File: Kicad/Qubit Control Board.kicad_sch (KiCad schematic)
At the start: 148 parts, among them J1 USB_C_Receptacle_PowerOnly_6P, J2 CLK_Pins, J3 Idata, J4 Qdata, J5 SPIdata, J6 SMA, U1 LT3045xMSE, U2 TRF372017IRGZR, U3 LT3045xMSE, U4 LT3045xMSE, U5 SN65LVDS1DBV, U6 AD9743BCPZ, Y2 CVHD-950-100.000

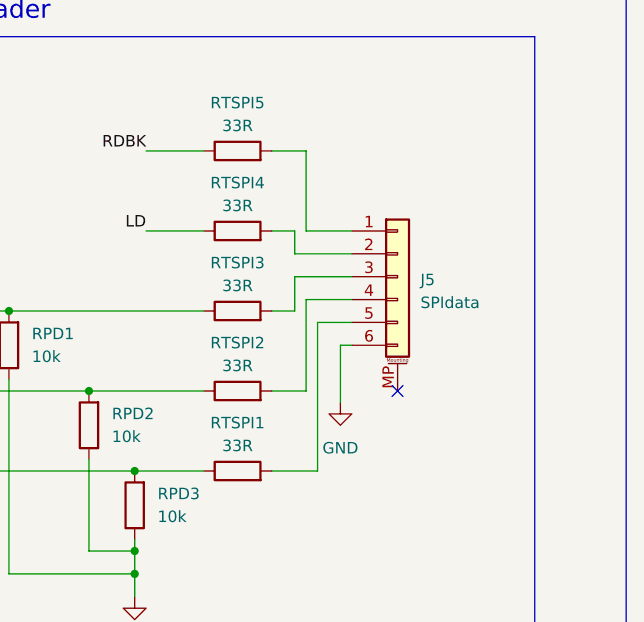
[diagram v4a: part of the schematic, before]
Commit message: Did 3.3V-B LDO routing
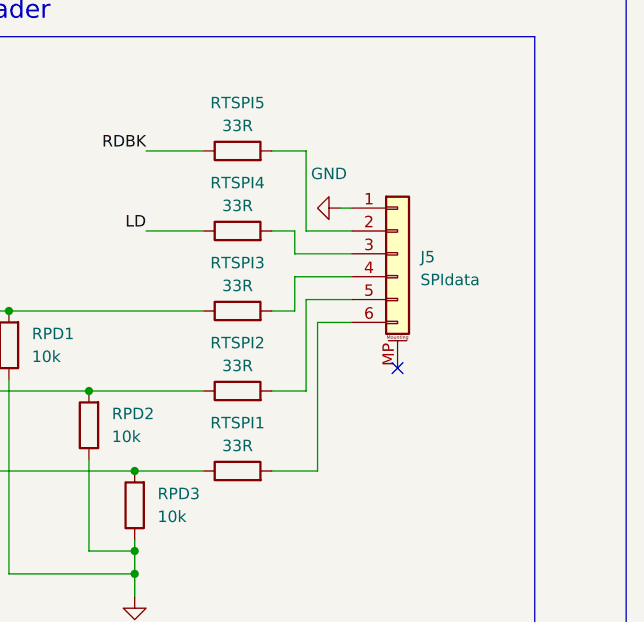
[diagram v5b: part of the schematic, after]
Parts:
- CD11, CD20, CD21, CD22, CD26: footprint Capacitor_SMD:C_0805_2012Metric_Pad1.18x1.45mm_HandSolder -> Capacitor_SMD:C_0603_1608Metric
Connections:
- net GND: now also J5.1 (Pin_1); no longer J5.6 (Pin_6)
- net at RTSPI4.2: now also J5.3 (Pin_3); no longer J5.2 (Pin_2)
- net at RTSPI5.2: now also J5.2 (Pin_2); no longer J5.1 (Pin_1)
- net at RTSPI1.2: now also J5.6 (Pin_6); no longer J5.5 (Pin_5)
- net at RTSPI3.2: now also J5.4 (Pin_4); no longer J5.3 (Pin_3)
- net at RTSPI2.2: now also J5.5 (Pin_5); no longer J5.4 (Pin_4)
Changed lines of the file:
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@@
 	)
 	(no_connect
-		(at 551.18 255.27)
+		(at 551.18 252.73)
 	)
 	(no_connect
@@
 	(wire
 		(pts
-			(xy 546.1 250.19) (xy 544.83 250.19)
-		)
-		(stroke
-			(width 0)
-			(type default)
-		)
-	)
-	(wire
-		(pts
 			(xy 238.76 210.82) (xy 246.38 210.82)
 		)
@@
 	(wire
 		(pts
+			(xy 544.83 234.95) (xy 546.1 234.95)
+		)
+		(stroke
+			(width 0)
+			(type default)
+		)
+	)
+	(wire
+		(pts
 			(xy 508 107.95) (xy 501.65 107.95)
 		)
@@
 	(wire
 		(pts
-			(xy 544.83 250.19) (xy 544.83 256.54)
-		)
-		(stroke
-			(width 0)
-			(type default)
-		)
-	)
-	(wire
-		(pts
 			(xy 210.82 130.81) (xy 209.55 130.81)
 		)
@@
 			)
 		)
-		(property "Footprint" "Capacitor_SMD:C_0805_2012Metric_Pad1.18x1.45mm_HandSolder"
+		(property "Footprint" "Capacitor_SMD:C_0603_1608Metric"
 			(at 374.9548 256.54 0)
 			(hide yes)
@@
 			)
 		)
-		(property "Footprint" "Capacitor_SMD:C_0805_2012Metric_Pad1.18x1.45mm_HandSolder"
+		(property "Footprint" "Capacitor_SMD:C_0603_1608Metric"
 			(at 430.8348 287.02 0)
 			(hide yes)
@@
 	)
 	(symbol
-		(lib_id "Connector_Generic_MountingPin:Conn_01x06_MountingPin")
-		(at 551.18 242.57 0)
-		(unit 1)
-		(body_style 1)
-		(exclude_from_sim no)
-		(in_bom yes)
-		(on_board yes)
-		(in_pos_files yes)
-		(dnp no)
-		(fields_autoplaced yes)
-		(property "Reference" "J5"
-			(at 553.72 242.9255 0)
-			(show_name no)
-			(do_not_autoplace no)
-			(effects
-				(font
-					(size 1.27 1.27)
-				)
-				(justify left)
-			)
-		)
-		(property "Value" "SPIdata"
-			(at 553.72 245.4655 0)
-			(show_name no)
-			(do_not_autoplace no)
-			(effects
-				(font
-					(size 1.27 1.27)
-				)
-				(justify left)
-			)
-		)
-		(property "Footprint" "Connector_PinHeader_1.00mm:PinHeader_1x06_P1.00mm_Vertical"
-			(at 551.18 242.57 0)
-			(hide yes)
-			(show_name no)
-			(do_not_autoplace no)
-			(effects
-				(font
-					(size 1.27 1.27)
-				)
-			)
-		)
-		(property "Datasheet" ""
-			(at 551.18 242.57 0)
-			(hide yes)
-			(show_name no)
-			(do_not_autoplace no)
-			(effects
-				(font
-					(size 1.27 1.27)
-				)
-			)
-		)
-		(property "Description" "Generic connectable mounting pin connector, single row, 01x06, script generated (kicad-library-utils/schlib/autogen/connector/)"
-			(at 551.18 242.57 0)
-			(hide yes)
-			(show_name no)
-			(do_not_autoplace no)
-			(effects
-				(font
-					(size 1.27 1.27)
-				)
-			)
-		)
-		(pin "5"
-		)
-		(pin "6"
-		)
-		(pin "4"
-		)
-		(pin "2"
-		)
-		(pin "3"
-		)
-		(pin "1"
-		)
-		(pin "MP"
-		)
-		(instances
-			(project "Qubit Control Board"
-				(path "/d02a9e30-46b8-444a-9e12-1a93fb154b6d"
-					(reference "J5")
-					(unit 1)
-				)
-			)
-		)
-	)
-	(symbol
 		(lib_id "power:GND")
 		(at 54.61 106.68 0)
@@
 			)
 		)
-		(property "Footprint" "Capacitor_SMD:C_0805_2012Metric_Pad1.18x1.45mm_HandSolder"
+		(property "Footprint" "Capacitor_SMD:C_0603_1608Metric"
 			(at 374.9548 287.02 0)
 			(hide yes)
@@
 			)
 		)
-		(property "Footprint" "Capacitor_SMD:C_0805_2012Metric_Pad1.18x1.45mm_HandSolder"
+		(property "Footprint" "Capacitor_SMD:C_0603_1608Metric"
 			(at 484.1748 322.58 0)
 			(hide yes)
@@
 	(symbol
 		(lib_id "power:GND")
-		(at 544.83 256.54 0)
+		(at 544.83 234.95 270)
 		(unit 1)
 		(body_style 1)
@@
 		(fields_autoplaced yes)
 		(property "Reference" "#PWR058"
-			(at 544.83 262.89 0)
+			(at 538.48 234.95 0)
 			(hide yes)
 			(show_name no)
@@
 		)
 		(property "Value" "GND"
-			(at 544.83 261.62 0)
+			(at 543.56 231.14 90)
 			(show_name no)
 			(do_not_autoplace no)
@@
 		)
 		(property "Footprint" ""
-			(at 544.83 256.54 0)
+			(at 544.83 234.95 0)
 			(hide yes)
 			(show_name no)
@@
 		)
 		(property "Datasheet" ""
-			(at 544.83 256.54 0)
+			(at 544.83 234.95 0)
 			(hide yes)
 			(show_name no)
@@
 		)
 		(property "Description" "Power symbol creates a global label with name \"GND\" , ground"
-			(at 544.83 256.54 0)
+			(at 544.83 234.95 0)
 			(hide yes)
 			(show_name no)
@@
 			)
 		)
-		(property "Footprint" "Capacitor_SMD:C_0805_2012Metric_Pad1.18x1.45mm_HandSolder"
+		(property "Footprint" "Capacitor_SMD:C_0603_1608Metric"
 			(at 432.1048 256.54 0)
 			(hide yes)
@@
 					(unit 1)
 				)
+			)
+		)
+	)
+	(symbol
+		(lib_id "Connector_Generic_MountingPin:Conn_01x06_MountingPin")
+		(at 551.18 240.03 0)
+		(unit 1)
+		(body_style 1)
+		(exclude_from_sim no)
+		(in_bom yes)
+		(on_board yes)
+		(in_pos_files yes)
+		(dnp no)
+		(fields_autoplaced yes)
+		(property "Reference" "J5"
+			(at 553.72 240.3855 0)
+			(show_name no)
+			(do_not_autoplace no)
+			(effects
+				(font
+					(size 1.27 1.27)
+				)
+				(justify left)
+			)
+		)
+		(property "Value" "SPIdata"
+			(at 553.72 242.9255 0)
+			(show_name no)
+			(do_not_autoplace no)
+			(effects
+				(font
+					(size 1.27 1.27)
+				)
+				(justify left)
+			)
+		)
+		(property "Footprint" "Connector_PinHeader_1.00mm:PinHeader_1x06_P1.00mm_Vertical"
+			(at 551.18 240.03 0)
+			(hide yes)
+			(show_name no)
+			(do_not_autoplace no)
+			(effects
+				(font
+					(size 1.27 1.27)
+				)
+			)
+		)
+		(property "Datasheet" ""
+			(at 551.18 240.03 0)
+			(hide yes)
+			(show_name no)
+			(do_not_autoplace no)
+			(effects
+				(font
+					(size 1.27 1.27)
+				)
+			)
+		)
+		(property "Description" "Generic connectable mounting pin connector, single row, 01x06, script generated (kicad-library-utils/schlib/autogen/connector/)"
+			(at 551.18 240.03 0)
+			(hide yes)
+			(show_name no)
+			(do_not_autoplace no)
+			(effects
+				(font
+					(size 1.27 1.27)
+				)
+			)
+		)
+		(pin "5"
+		)
+		(pin "6"
+		)
+		(pin "4"
+		)
+		(pin "2"
+		)
+		(pin "3"
+		)
+		(pin "1"
+		)
+		(pin "MP"
+		)
+		(instances
+			(project "Qubit Control Board"
+				(path "/d02a9e30-46b8-444a-9e12-1a93fb154b6d"
+					(reference "J5")
+					(unit 1)
+				)

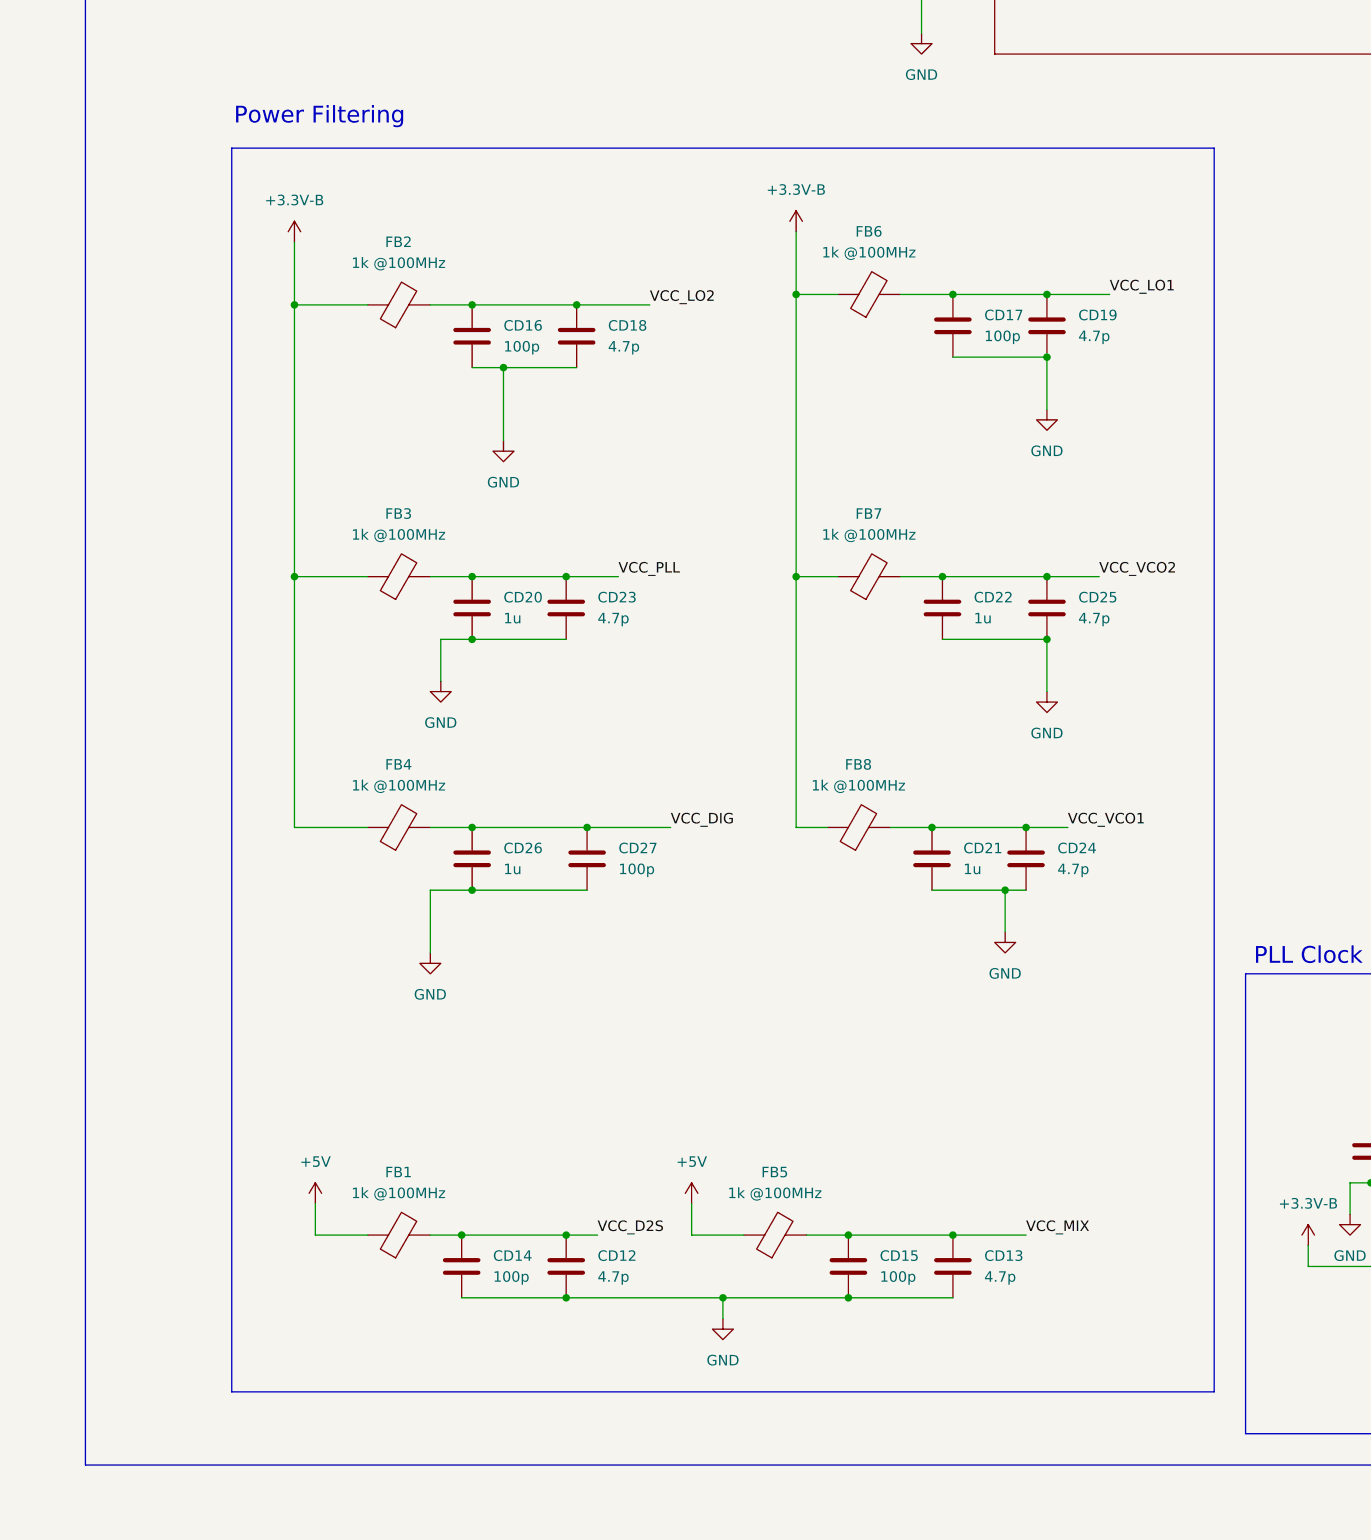
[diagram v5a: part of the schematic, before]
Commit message: Added 10n input caps to PLL power rails
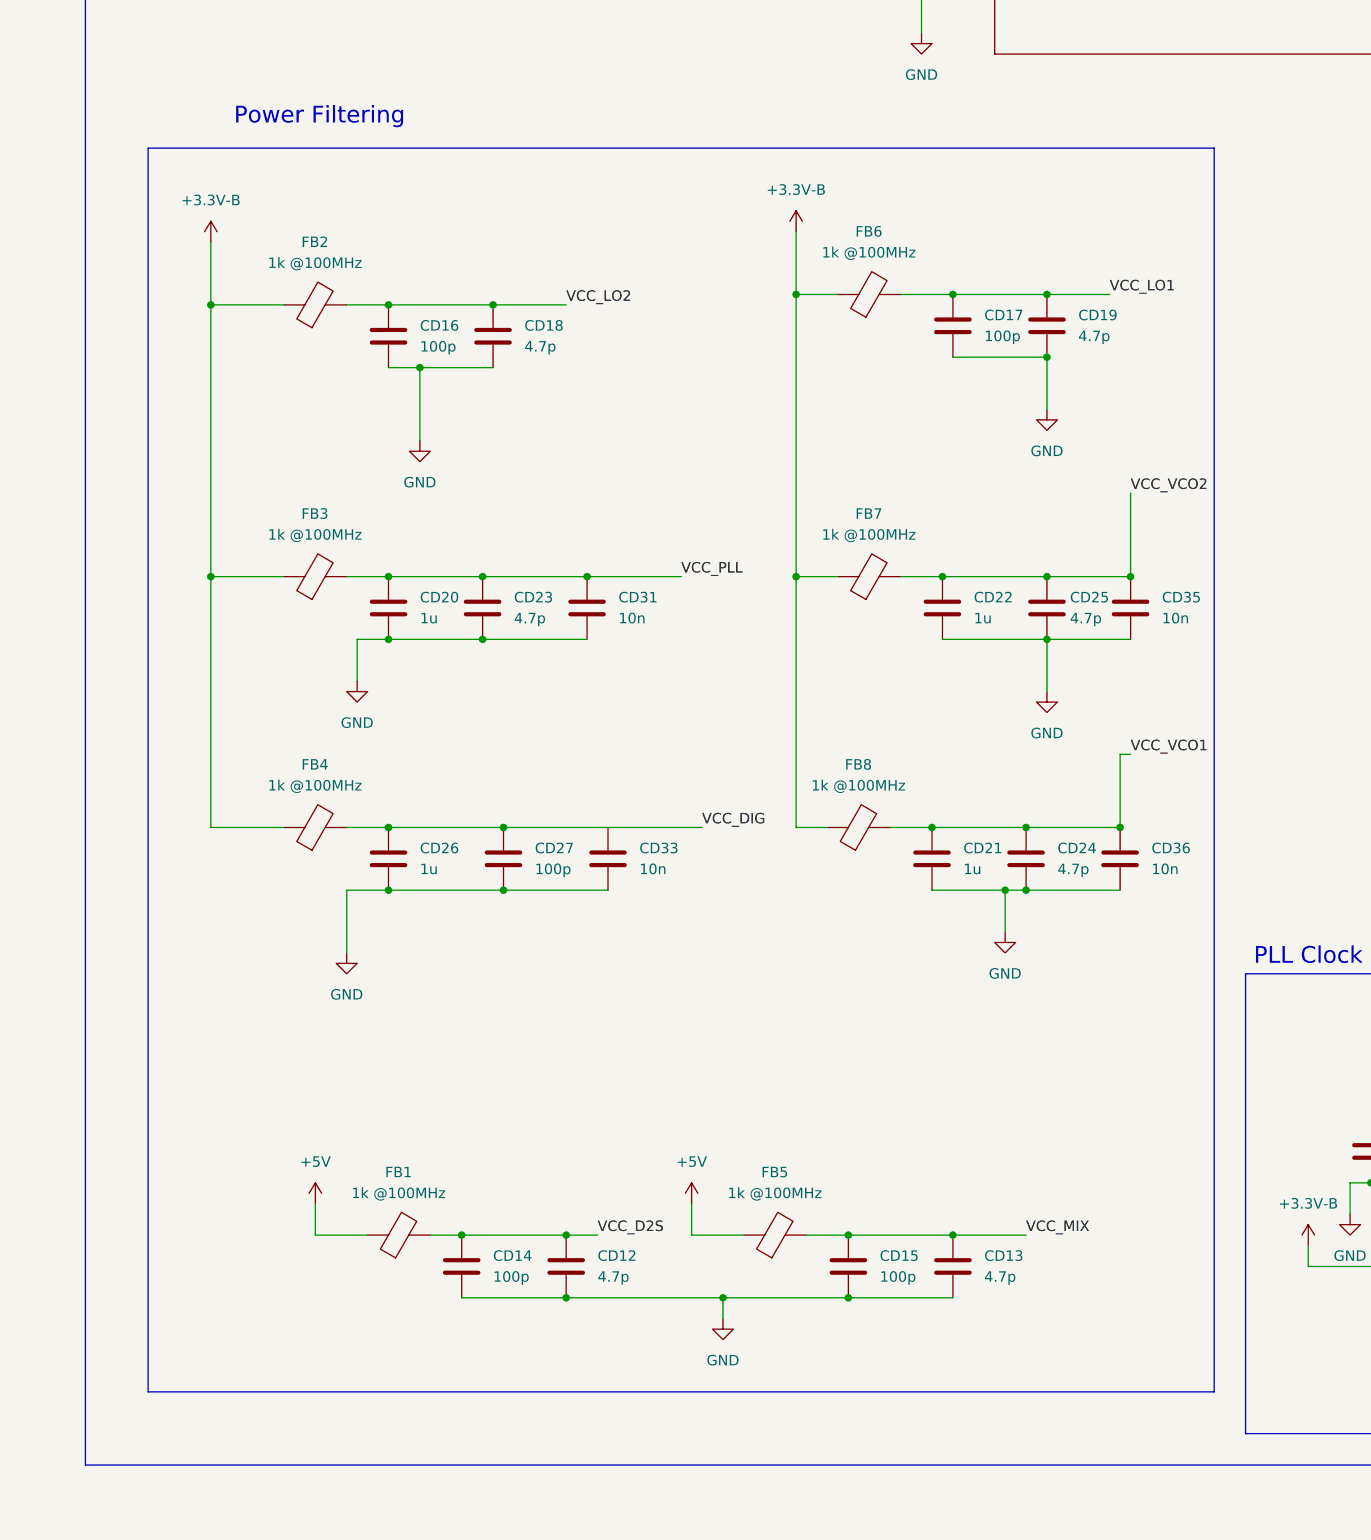
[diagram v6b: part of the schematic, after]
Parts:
- added CD31, CD33, CD35, CD36: 10n, Capacitor_SMD:C_0402_1005Metric, symbol Device:C
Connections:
- net GND: now also CD31.1, CD33.1, CD35.1, CD36.1
- net VCC_PLL: now also CD31.2
- net VCC_VCO1: now also CD36.2
- net VCC_VCO2: now also CD35.2
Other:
- moved on the sheet: CD16, CD18, CD20, CD23, CD26, CD27, FB2, FB3, FB4
